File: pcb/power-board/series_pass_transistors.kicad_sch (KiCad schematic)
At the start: 6 parts, among them Q40 BD249C, Q41 BD139, Q42 BD249C, Q43 BD139

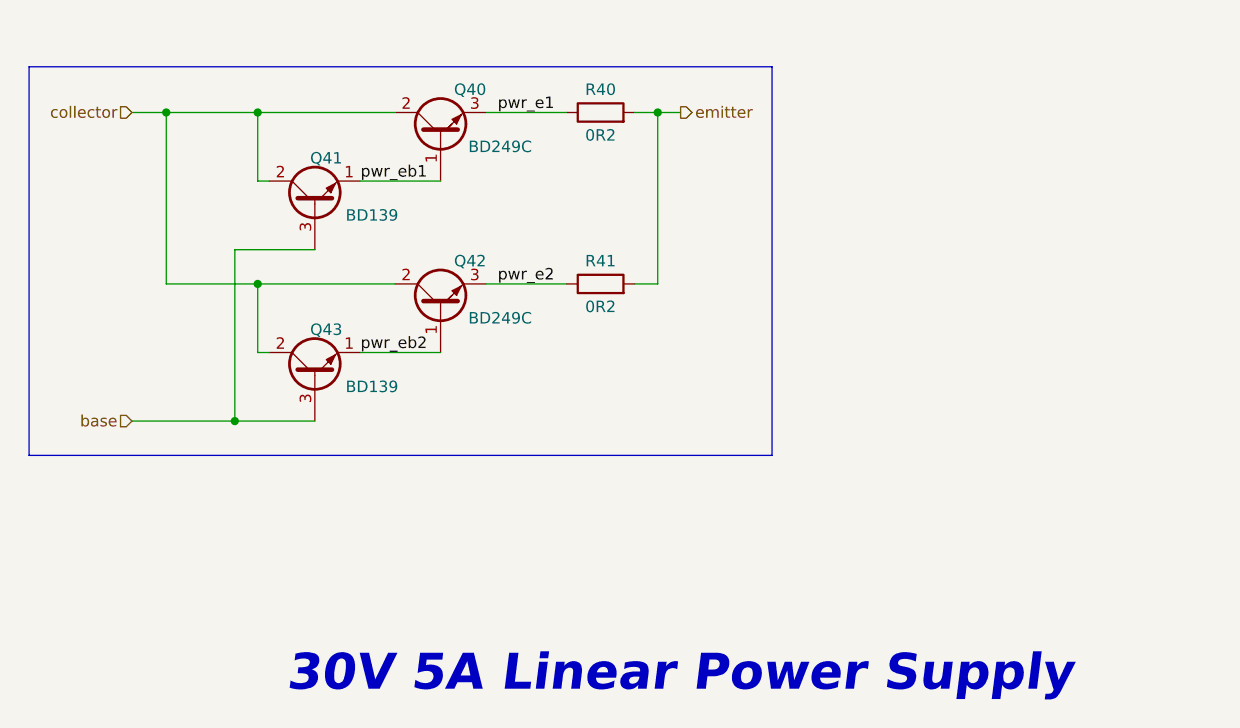
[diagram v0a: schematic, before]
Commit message: Perform minor stylistic changes on power-board schematic, clear DRC
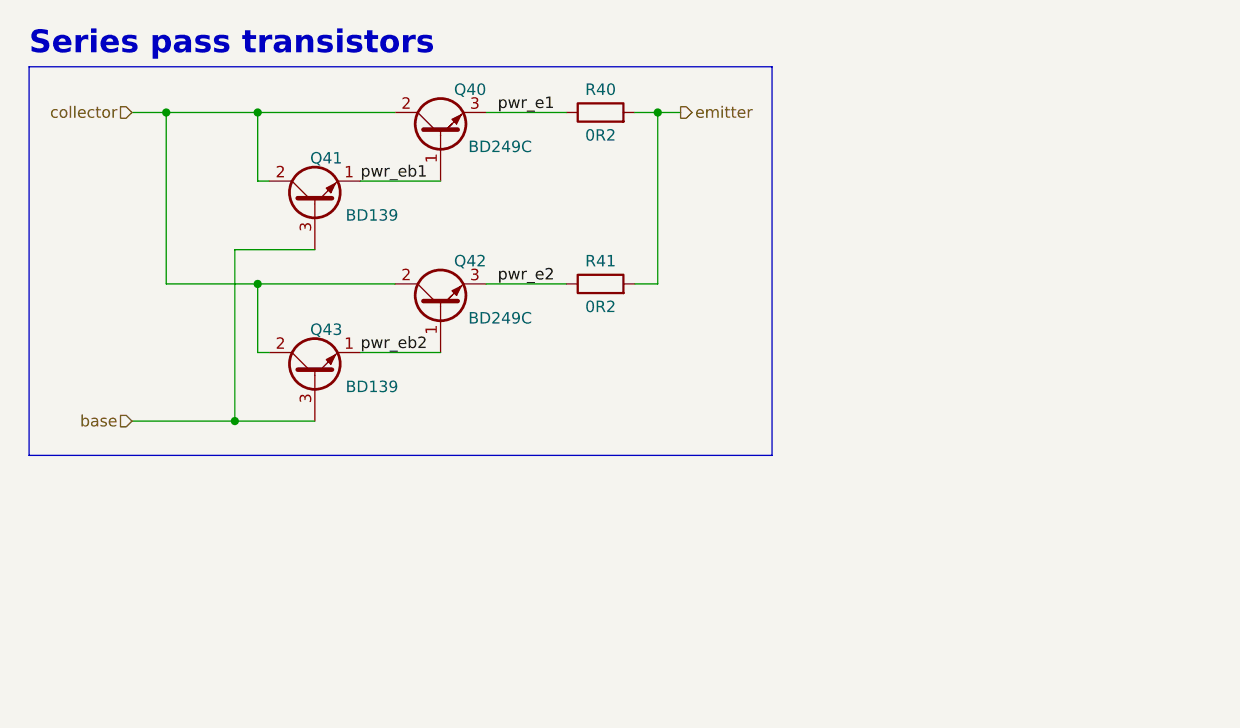
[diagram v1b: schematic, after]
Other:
- note added: "Series pass transistors"
- note removed: "30V 5A Linear Power Supply"
- title: Series pass transistors -> DW3005T-power-board
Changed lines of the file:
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@@
 	(paper "A5")
 	(title_block
-		(title "Series pass transistors")
-		(date "2024-02-24")
-		(rev "V1.0")
+		(title "DW3005T-power-board")
+		(date "2024-02-26")
+		(rev "1.0.0")
 		(company "Dominik Workshop")
 	)
@@
 		)
 	)
-	(text "30V 5A Linear Power Supply"
+	(text "Series pass transistors"
 		(exclude_from_sim no)
-		(at 95.885 114.3 0)
+		(at 67.31 41.91 0)
 		(effects
 			(font
-				(size 4 4)
-				(thickness 0.8)
+				(size 2.54 2.54)
+				(thickness 0.508)
 				(bold yes)
-				(italic yes)
 			)
-			(justify left bottom)
-		)
-	)
+			(justify left)
+		)
+	)
